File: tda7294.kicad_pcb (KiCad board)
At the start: 2 copper layers, 100 x 48 mm, 62 parts, among them J1 Screw_Terminal_01x04, J2 Screw_Terminal_01x04, J3 Screw_Terminal_01x02, J4 Screw_Terminal_01x03, Q1 BSS84, Q2 2N7002, U1 TDA7293, U2 TDA7293, U3 PC817, U4 MCP1792

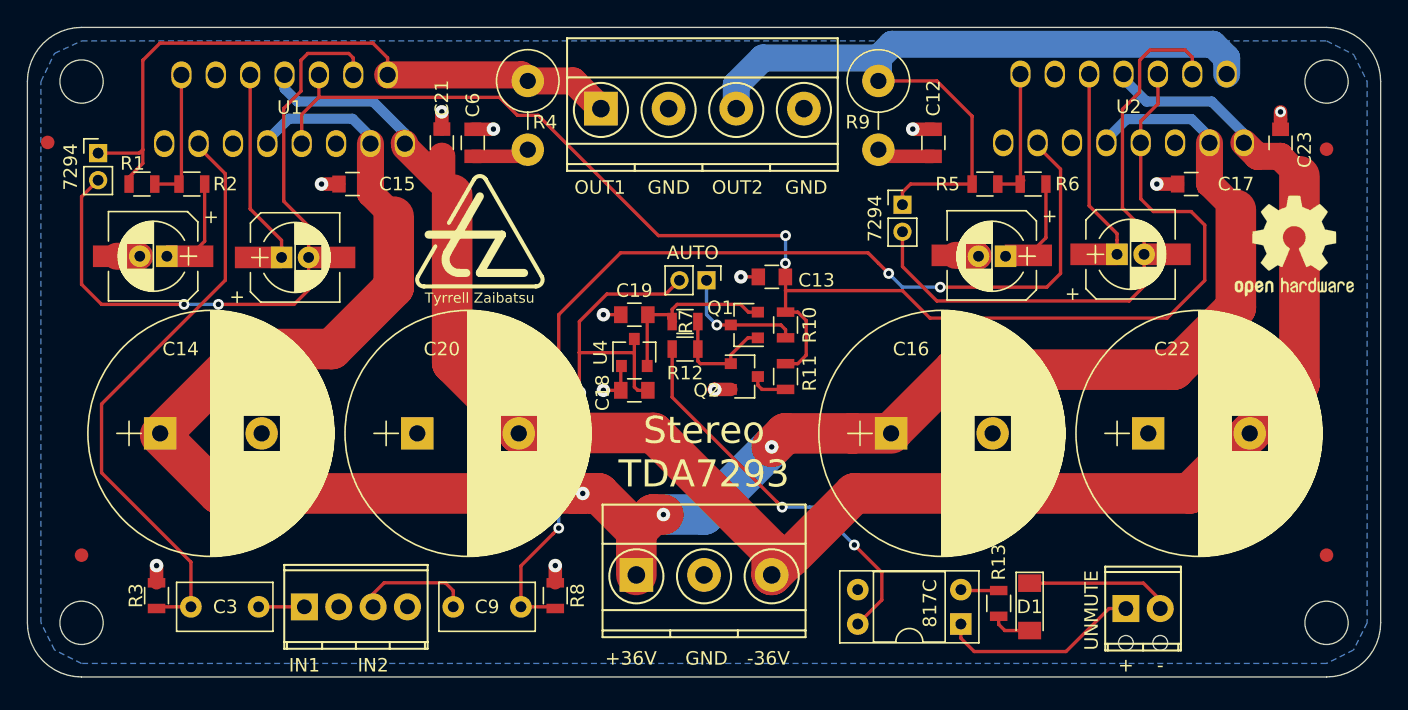
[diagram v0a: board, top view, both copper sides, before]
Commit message: Re-routed to separate the signal, power and output grounds
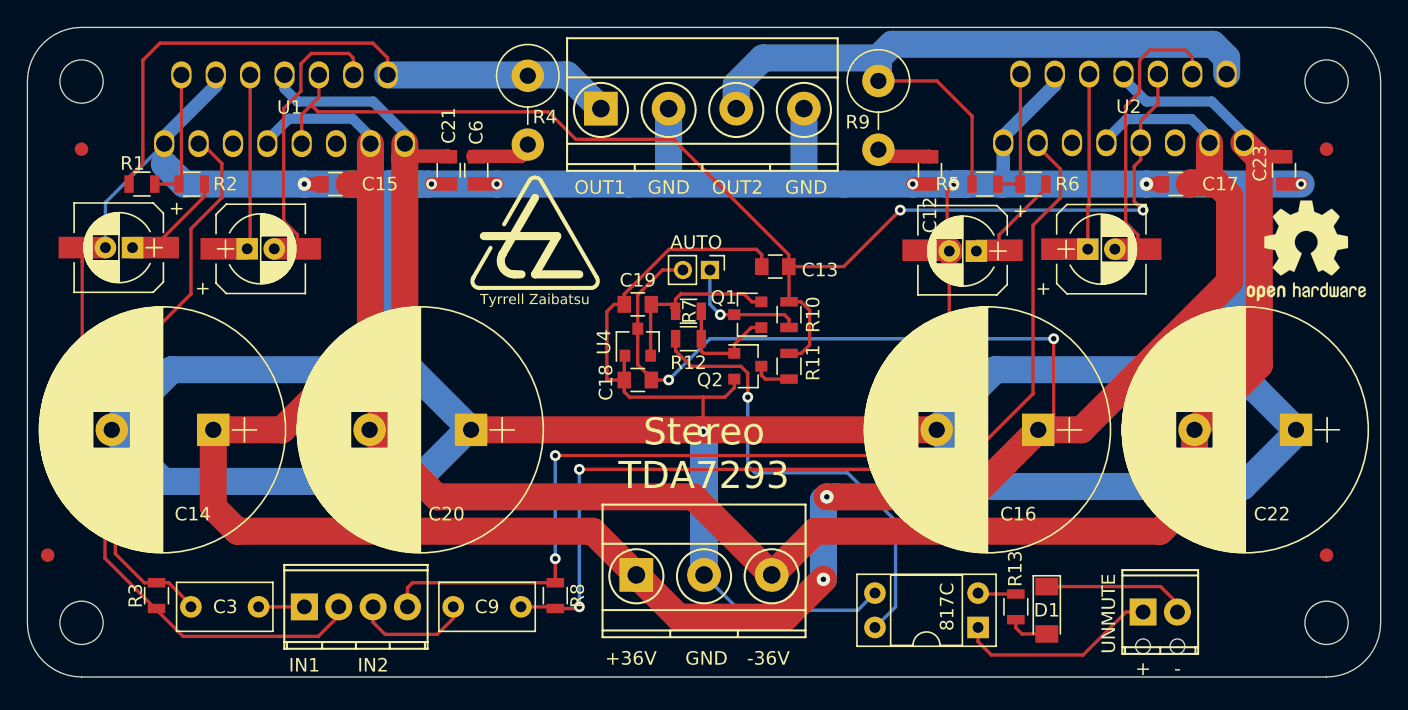
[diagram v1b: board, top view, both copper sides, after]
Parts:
- removed JP1, JP2: Jumper_NO_Small, Pin_Headers:Pin_Header_Straight_1x02_Pitch2.00mm
- moved C22 10.9 mm to (118.7, 54.7), turned to 180 degrees
- moved C16 10.9 mm to (99.7, 54.7), turned to 180 degrees
- moved REF** 8.05 mm to (75.5, 53.5)
- moved REF** 4.08 mm to (62.5, 41.0)
- moved C20 3.98 mm to (57.8, 54.7), turned to 180 degrees
- moved C14 3.93 mm to (38.7, 54.7), turned to 180 degrees
- moved REF*** 3.93 mm to (106.0, 61.0)
- moved C1 2.62 mm to (31.8, 41.3)
- moved C2 2.62 mm to (32.8, 41.3)
- moved C4 2.62 mm to (42.2, 41.4)
- moved C5 2.62 mm to (41.2, 41.4)
- moved FID2 2.55 mm to (29.0, 34.0)
- moved FID4 2.50 mm to (26.5, 64.0)
- moved C10 2.19 mm to (104.4, 41.4)
- moved C11 2.19 mm to (103.4, 41.4)
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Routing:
- net /GND: track 21.6 -> 506.2 mm, vias 12 -> 10
- net Net-(C4-Pad2): track 51.6 -> 20.2 mm, vias 2 -> 0
- net Net-(C10-Pad2): track 45.5 -> 20.5 mm
- net /VCC: track 189.8 -> 209.5 mm
- net /MUTE: track 108.5 -> 94.8 mm
- net /VEE: track 138.3 -> 149.6 mm
- net /OUT2: track 61.9 -> 55.6 mm
- net Net-(R12-Pad1): track 29.0 -> 34.9 mm, vias 2 -> 1
- net Net-(C9-Pad1): track 76.1 -> 70.5 mm, vias 4 -> 2
- net /OUT1: track 50.1 -> 46.7 mm
- net Net-(C4-Pad1): track 16.2 -> 13.6 mm
- net Net-(C1-Pad1): track 7.70 -> 5.81 mm
- net Net-(C10-Pad1): track 14.2 -> 13.0 mm
- net Net-(C7-Pad1): track 7.52 -> 8.03 mm
- net Net-(C3-Pad1): track 44.2 -> 44.7 mm
- removed copper zone on B.Cu, net /GND
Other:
- board text added: "Stereo TDA7293 Rev.A 202111 william@brodie-tyrrell.org github.com/phenidone"
- board text removed: "7294"
- board text removed: "Stereo TDA7293/TDA7294 Rev.A 202111 william@brodie-tyrrell.org github.com/phenidone"
